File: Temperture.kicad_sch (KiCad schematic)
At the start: 0 parts

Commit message: Стартовая версия
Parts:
- added C3, C4: 100n, Capacitor_SMD:C_0805_2012Metric_Pad1.18x1.45mm_HandSolder, symbol Device:C_Small
- added R2: 10k, Resistor_SMD:R_0805_2012Metric_Pad1.20x1.40mm_HandSolder, symbol Device:R
- added TH1: 10k, Resistor_SMD:R_1206_3216Metric_Pad1.30x1.75mm_HandSolder, symbol Device:Thermistor_NTC
- added U1: AD8603, Package_TO_SOT_SMD:TSOT-23-5, symbol Amplifier_Operational:AD8603
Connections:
- new net: C3.1, R2.2, TH1.1, U1.3 (+)
- new net +5V: C4.1, R2.1, U1.5 (V+)
- new net GND: C3.2, C4.2, TH1.2, U1.2 (V-)
- new net Temp_out: U1.1, U1.4 (-)

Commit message: Стартовая версия
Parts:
- added C10, C11, C8, C9: 100n, Capacitor_SMD:C_0805_2012Metric_Pad1.18x1.45mm_HandSolder, symbol Device:C_Small
- added R11, R12: 10k, Resistor_SMD:R_0805_2012Metric_Pad1.20x1.40mm_HandSolder, symbol Device:R
- added TH2, TH3: 10k, Resistor_SMD:R_1206_3216Metric_Pad1.30x1.75mm_HandSolder, symbol Device:Thermistor_NTC
- added U3, U4: AD8603, Package_TO_SOT_SMD:TSOT-23-5, symbol Amplifier_Operational:AD8603
- renumbered C3 to C4, C4 to C5, R2 to R10, U1 to U2
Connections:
- net +5V: now also C11.1, C9.1, R11.1, R12.1, U3.5 (V+), U4.5 (V+)
- net GND: now also C10.2, C11.2, C8.2, C9.2, TH2.2, TH3.2, U3.2 (V-), U4.2 (V-)
- net Temp_out renamed Temp_B
- new net: C10.1, R12.2, TH3.1, U4.3 (+)
- new net: C8.1, R11.2, TH2.1, U3.3 (+)
- new net Temp_A: U4.1, U4.4 (-)
- new net Temp_C: U3.1, U3.4 (-)
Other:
- moved on the sheet: C4, C5, R10, TH1, U2

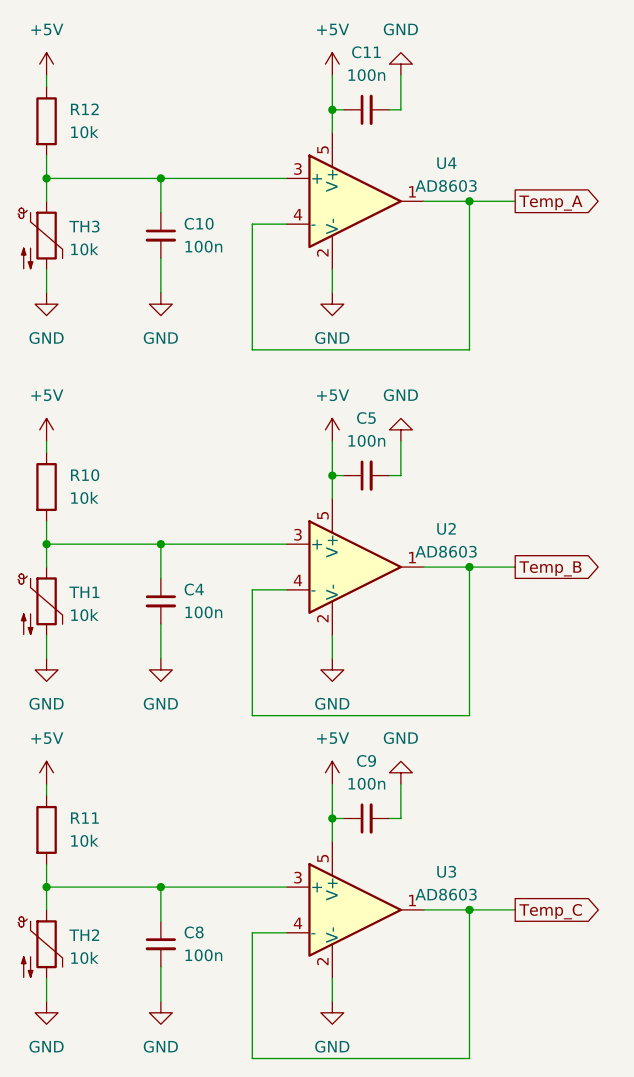
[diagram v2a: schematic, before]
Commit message: Перенес защиту от переполюсовки и добавил керамику
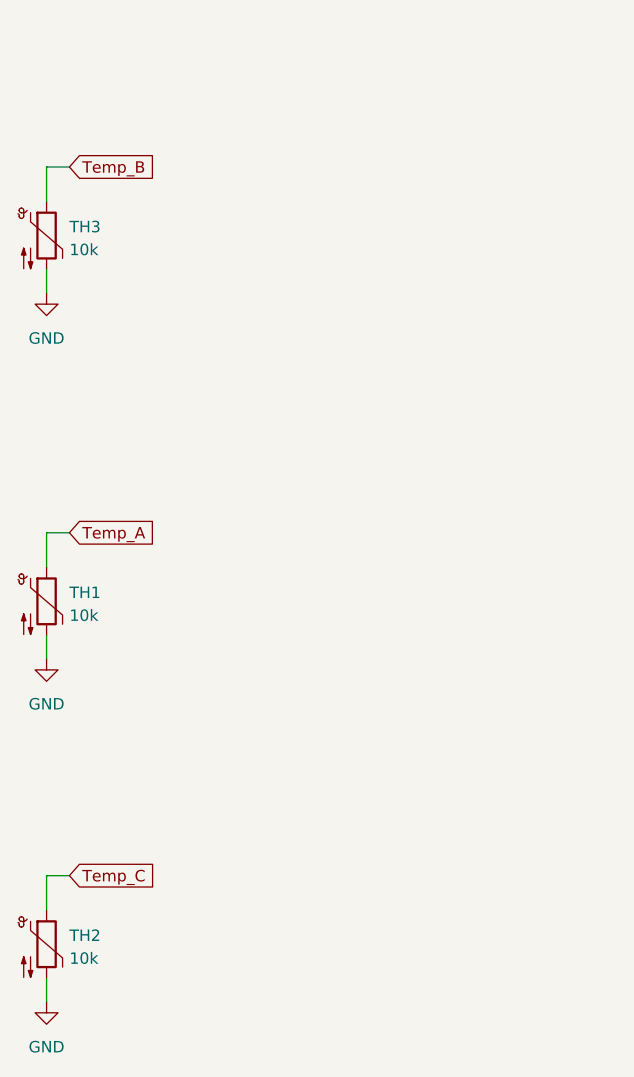
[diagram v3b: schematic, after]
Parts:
- removed C10, C11, C4, C5, C8, C9: 100n, Capacitor_SMD:C_0805_2012Metric_Pad1.18x1.45mm_HandSolder, symbol Device:C_Small
- removed R10, R11, R12: 10k, Resistor_SMD:R_0805_2012Metric_Pad1.20x1.40mm_HandSolder, symbol Device:R
- removed U2, U3, U4: AD8603, Package_TO_SOT_SMD:TSOT-23-5, symbol Amplifier_Operational:AD8603
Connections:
- net Temp_A: now also TH1.1
- net Temp_B: now also TH3.1
- net Temp_C: now also TH2.1

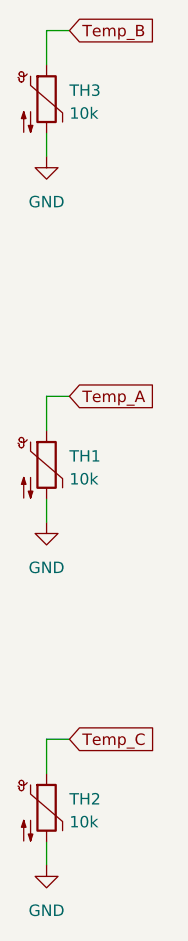
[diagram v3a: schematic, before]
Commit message: Поставил керамические Y конденсаторы
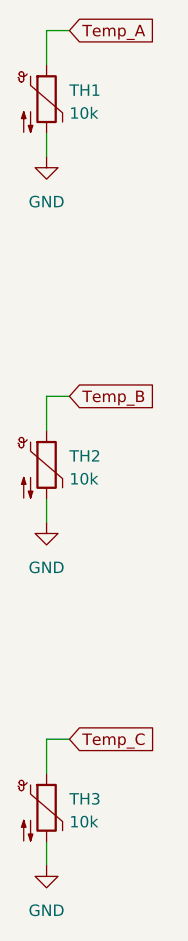
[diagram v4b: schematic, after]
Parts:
- renumbered TH3 to TH1, TH1 to TH2, TH2 to TH3
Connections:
- net Temp_A: now also TH1.1; no longer TH2.1
- net Temp_B: now also TH2.1; no longer TH1.1
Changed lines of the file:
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@@
     (stroke (width 0) (type default))
   )
-  (global_label "Temp_B" (shape input) (at 116.84 53.34 0) (fields_autoplaced)
+  (global_label "Temp_A" (shape input) (at 116.84 53.34 0) (fields_autoplaced)
     (effects (font (size 1.27 1.27)) (justify left))
-    (property "Intersheetrefs" "${INTERSHEET_REFS}" (at 126.9613 53.34 0)
+    (property "Intersheetrefs" "${INTERSHEET_REFS}" (at 126.7799 53.34 0)
       (effects (font (size 1.27 1.27)) (justify left) hide)
     )
@@
     )
   )
-  (global_label "Temp_A" (shape input) (at 116.84 93.98 0) (fields_autoplaced)
+  (global_label "Temp_B" (shape input) (at 116.84 93.98 0) (fields_autoplaced)
     (effects (font (size 1.27 1.27)) (justify left))
-    (property "Intersheetrefs" "${INTERSHEET_REFS}" (at 126.7799 93.98 0)
+    (property "Intersheetrefs" "${INTERSHEET_REFS}" (at 126.9613 93.98 0)
       (effects (font (size 1.27 1.27)) (justify left) hide)
     )
@@
   (symbol (lib_id "power:GND") (at 114.3 67.31 0) (unit 1)
     (in_bom yes) (on_board yes) (dnp no) (fields_autoplaced)
-    (property "Reference" "#PWR035" (at 114.3 73.66 0)
+    (property "Reference" "#PWR025" (at 114.3 73.66 0)
       (effects (font (size 1.27 1.27)) hide)
     )
@@
       (project "Силовая плата"
         (path "/96c6fc92-8ec6-44f7-b0dc-9ad8f1acea09/005a885b-ef5f-4b8c-934f-72ceac7d73e5"
-          (reference "#PWR035") (unit 1)
+          (reference "#PWR025") (unit 1)
         )
       )
@@
   (symbol (lib_id "Device:Thermistor_NTC") (at 114.3 139.7 0) (unit 1)
     (in_bom yes) (on_board yes) (dnp no) (fields_autoplaced)
-    (property "Reference" "TH2" (at 116.84 138.7475 0)
+    (property "Reference" "TH3" (at 116.84 138.7475 0)
       (effects (font (size 1.27 1.27)) (justify left))
     )
@@
       (project "Силовая плата"
         (path "/96c6fc92-8ec6-44f7-b0dc-9ad8f1acea09/005a885b-ef5f-4b8c-934f-72ceac7d73e5"
-          (reference "TH2") (unit 1)
+          (reference "TH3") (unit 1)
         )
       )
@@
   (symbol (lib_id "Device:Thermistor_NTC") (at 114.3 101.6 0) (unit 1)
     (in_bom yes) (on_board yes) (dnp no) (fields_autoplaced)
-    (property "Reference" "TH1" (at 116.84 100.6475 0)
+    (property "Reference" "TH2" (at 116.84 100.6475 0)
       (effects (font (size 1.27 1.27)) (justify left))
     )
@@
       (project "Силовая плата"
         (path "/96c6fc92-8ec6-44f7-b0dc-9ad8f1acea09/005a885b-ef5f-4b8c-934f-72ceac7d73e5"
-          (reference "TH1") (unit 1)
+          (reference "TH2") (unit 1)
         )
       )
@@
   (symbol (lib_id "Device:Thermistor_NTC") (at 114.3 60.96 0) (unit 1)
     (in_bom yes) (on_board yes) (dnp no) (fields_autoplaced)
-    (property "Reference" "TH3" (at 116.84 60.0075 0)
+    (property "Reference" "TH1" (at 116.84 60.0075 0)
       (effects (font (size 1.27 1.27)) (justify left))
     )
@@
       (project "Силовая плата"
         (path "/96c6fc92-8ec6-44f7-b0dc-9ad8f1acea09/005a885b-ef5f-4b8c-934f-72ceac7d73e5"
-          (reference "TH3") (unit 1)
+          (reference "TH1") (unit 1)
         )
       )
@@
   (symbol (lib_id "power:GND") (at 114.3 146.05 0) (unit 1)
     (in_bom yes) (on_board yes) (dnp no) (fields_autoplaced)
-    (property "Reference" "#PWR029" (at 114.3 152.4 0)
+    (property "Reference" "#PWR027" (at 114.3 152.4 0)
       (effects (font (size 1.27 1.27)) hide)
     )
@@
       (project "Силовая плата"
         (path "/96c6fc92-8ec6-44f7-b0dc-9ad8f1acea09/005a885b-ef5f-4b8c-934f-72ceac7d73e5"
-          (reference "#PWR029") (unit 1)
+          (reference "#PWR027") (unit 1)
         )
       )
@@
   (symbol (lib_id "power:GND") (at 114.3 107.95 0) (unit 1)
     (in_bom yes) (on_board yes) (dnp no) (fields_autoplaced)
-    (property "Reference" "#PWR021" (at 114.3 114.3 0)
+    (property "Reference" "#PWR026" (at 114.3 114.3 0)
       (effects (font (size 1.27 1.27)) hide)
     )
@@
       (project "Силовая плата"
         (path "/96c6fc92-8ec6-44f7-b0dc-9ad8f1acea09/005a885b-ef5f-4b8c-934f-72ceac7d73e5"
-          (reference "#PWR021") (unit 1)
+          (reference "#PWR026") (unit 1)
         )
       )

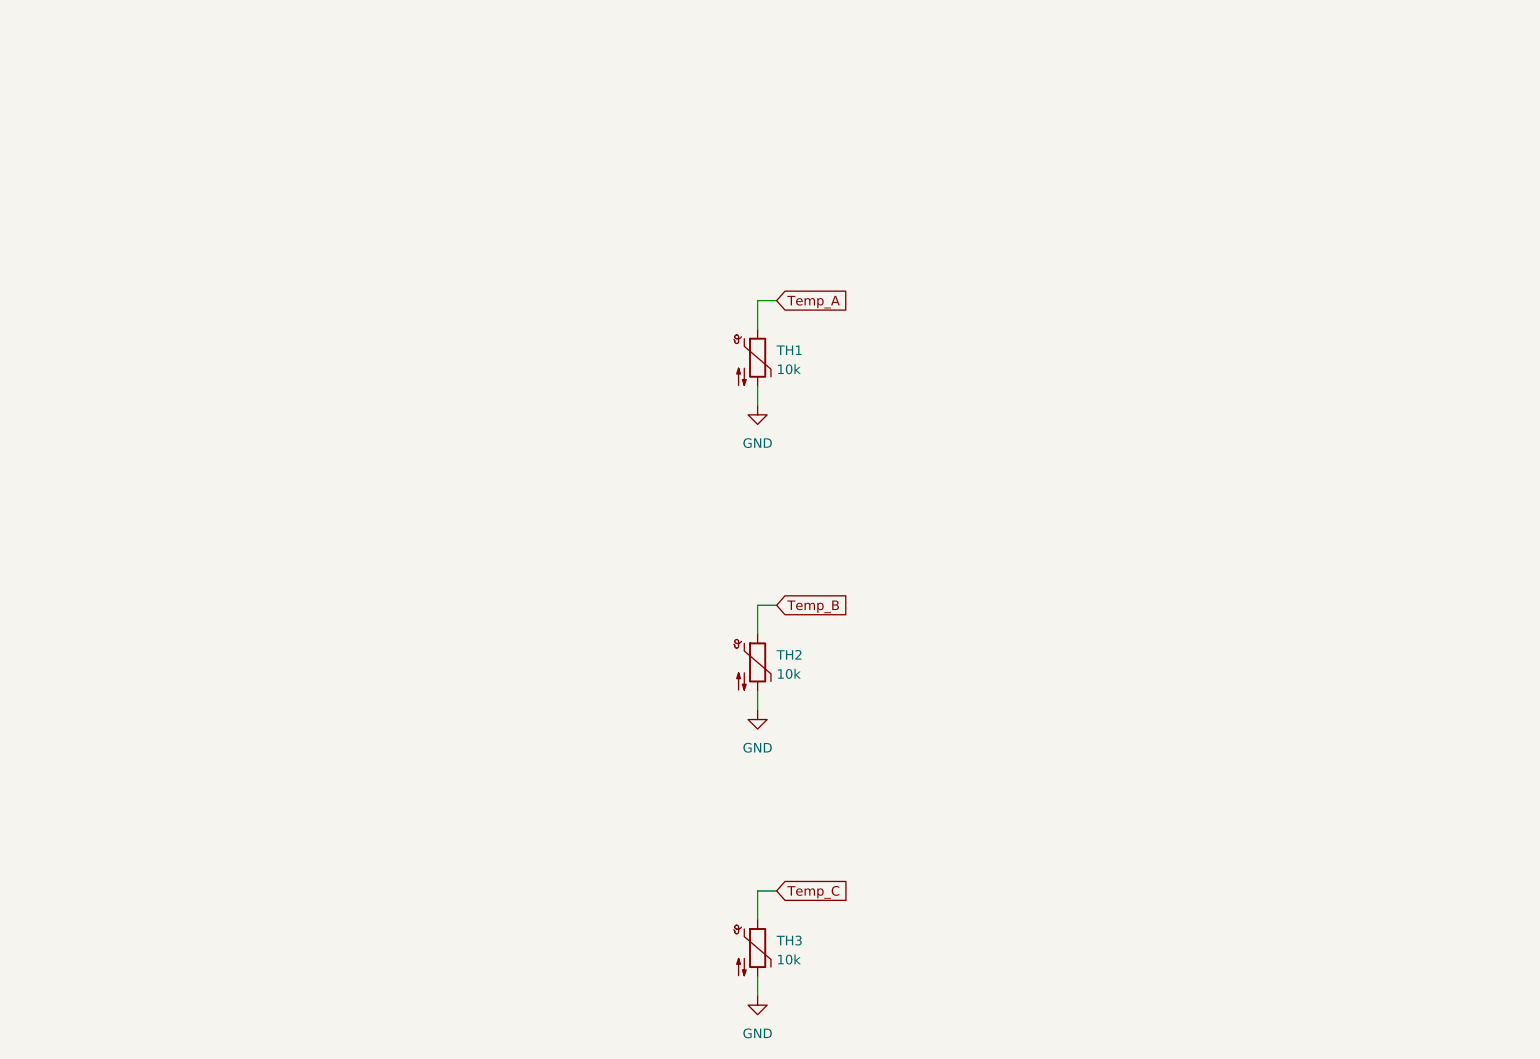
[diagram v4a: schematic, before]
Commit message: Поменял NTC на цифровые датчики
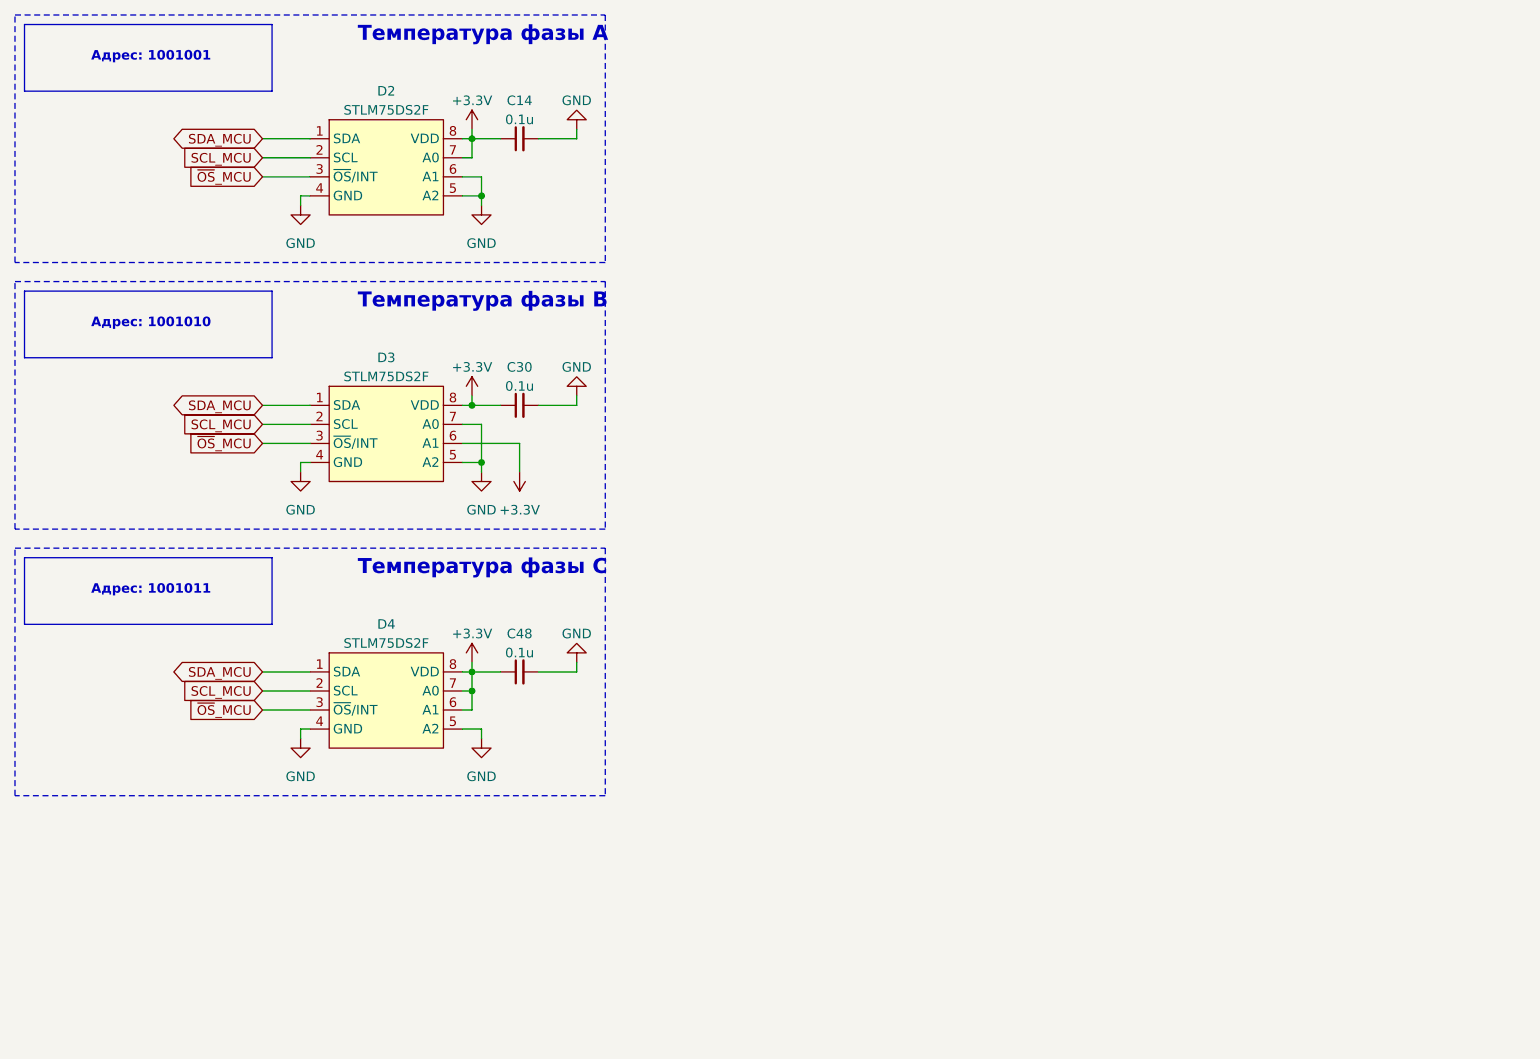
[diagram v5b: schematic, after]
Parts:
- removed TH1, TH2, TH3: 10k, Resistor_SMD:R_1206_3216Metric_Pad1.30x1.75mm_HandSolder, symbol Device:Thermistor_NTC
- added C14, C30, C48: 0.1u, Capacitor_SMD:C_0603_1608Metric_Pad1.08x0.95mm_HandSolder, symbol Device:C_Small
- added D2, D3, D4: STLM75DS2F, Package_SO:MSOP-8_3x3mm_P0.65mm, symbol Temperature_My:STLM75DS2F
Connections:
- net GND: now also C14.2, C30.2, C48.2, D2.4 (GND), D2.5 (A2), D2.6 (A1), D3.4 (GND), D3.5 (A2), D3.7 (A0), D4.4 (GND), D4.5 (A2)
- new net +3.3V: C14.1, C30.1, C48.1, D2.7 (A0), D2.8 (VDD), D3.6 (A1), D3.8 (VDD), D4.6 (A1), D4.7 (A0), D4.8 (VDD)
- new net SCL_MCU: D2.2 (SCL), D3.2 (SCL), D4.2 (SCL)
- new net SDA_MCU: D2.1 (SDA), D3.1 (SDA), D4.1 (SDA)
- new net ~{OS}_MCU: D2.3 (~{OS}/INT), D3.3 (~{OS}/INT), D4.3 (~{OS}/INT)
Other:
- note added: "Адрес: 1001001"
- note added: "Адрес: 1001010"
- note added: "Адрес: 1001011"
- note added: "Температура фазы А"
- note added: "Температура фазы В"
- note added: "Температура фазы С"
